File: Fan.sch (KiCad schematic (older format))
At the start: 0 parts

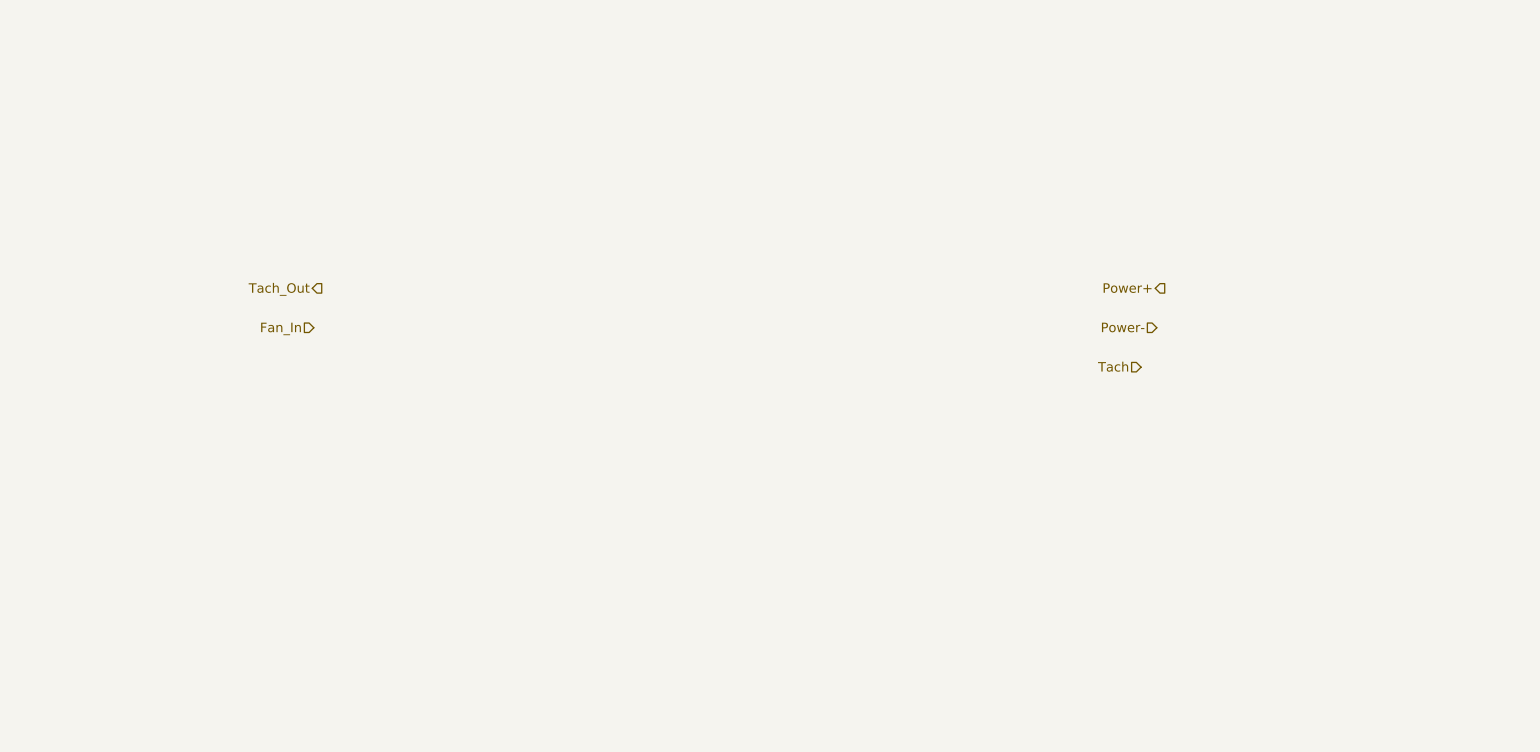
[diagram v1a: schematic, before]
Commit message: Added Fan control outline
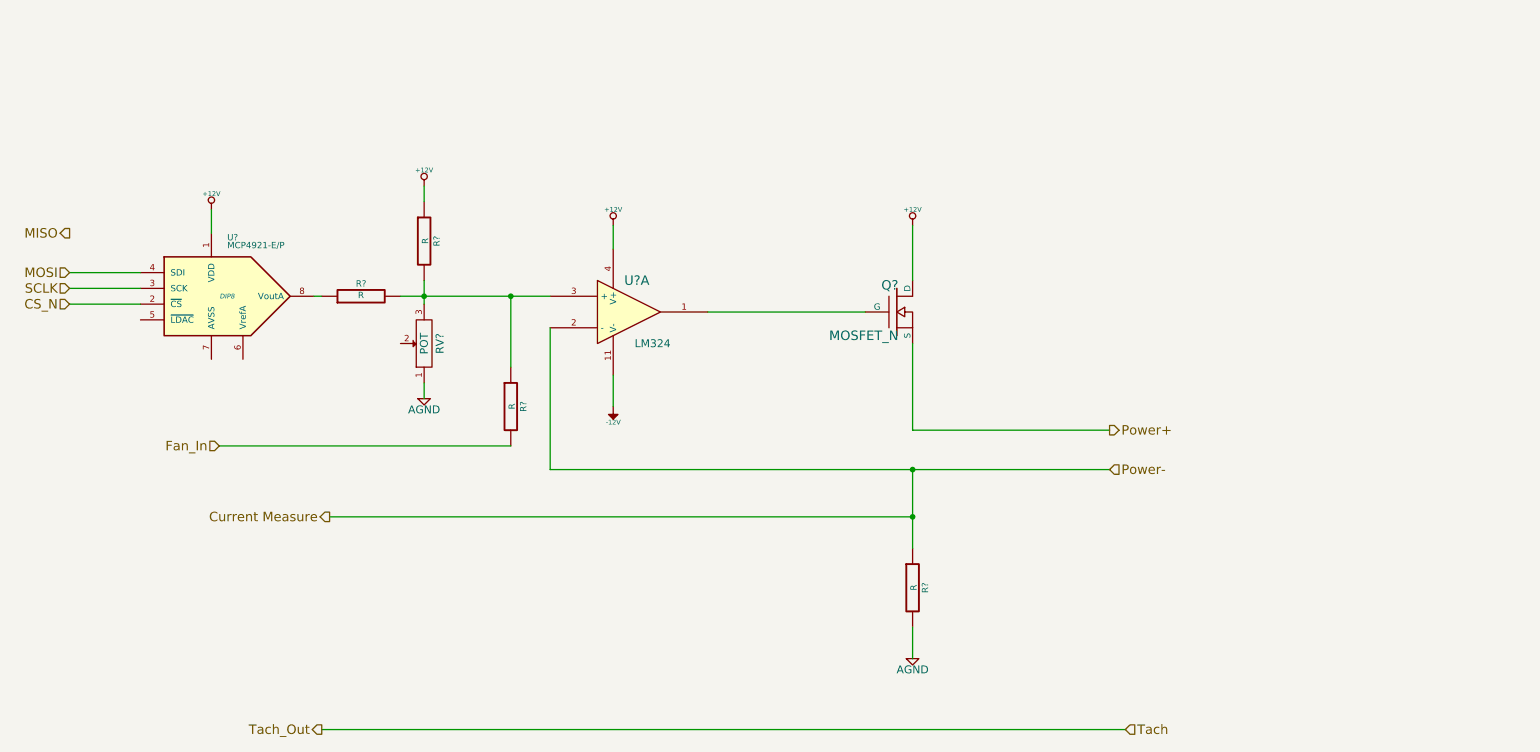
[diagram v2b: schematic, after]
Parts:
- added Q?: MOSFET_N, ~, symbol MOSFET_N
- added R? (x4): R, ~, symbol R
- added RV?: POT, ~, symbol POT
- added U?: LM324, symbol LM324
- added U?: MCP4921-E/P, DIP8, symbol MCP4921-E/P
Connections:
- net Fan_In: now also R?.2
- net Power+: now also Q?.S
- new net: Q?.G, U?.1
- new net: R?.1, R?.2, R?.2, RV?.3, U?.3 (+)
- new net: R?.1, U?.8 (VoutA)
- new net +12V: Q?.D, R?.1, U?.1 (VDD), U?.4 (V+)
- new net -12V: U?.11 (V-)
- new net AGND: R?.2, RV?.1
- new net CS_N: U?.2 (~CS~)
- new net Current Measure: R?.1, U?.2 (-)
- new net MOSI: U?.4 (SDI)
- new net SCLK: U?.3 (SCK)

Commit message: Hooked up top level schematic
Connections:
- net Current Measure renamed CURR_MEAS
- net Fan_In renamed FAN_EN_N
- net Power+ renamed FAN_OUT+
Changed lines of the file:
@@
 $EndDescr
 Text HLabel 7450 3300 2    60   Output ~ 0
-Power+
-Text HLabel 7450 3550 2    60   Input ~ 0
-Power-
+FAN_OUT+
+Text HLabel 7450 3550 2    60   Output ~ 0
+FAN_OUT-
 Text HLabel 7550 5200 2    60   Input ~ 0
-Tach
+TACH_IN
 Text HLabel 2450 5200 0    60   Output ~ 0
-Tach_Out
+TACH_MEAS
 Text HLabel 1800 3400 0    60   Input ~ 0
-Fan_In
+FAN_EN_N
 $Comp
 L LM324 U?
@@
 	2450 5200 7550 5200
 Text HLabel 2500 3850 0    60   Output ~ 0
-Current Measure
+CURR_MEAS
 Wire Wire Line
 	2500 3850 6200 3850

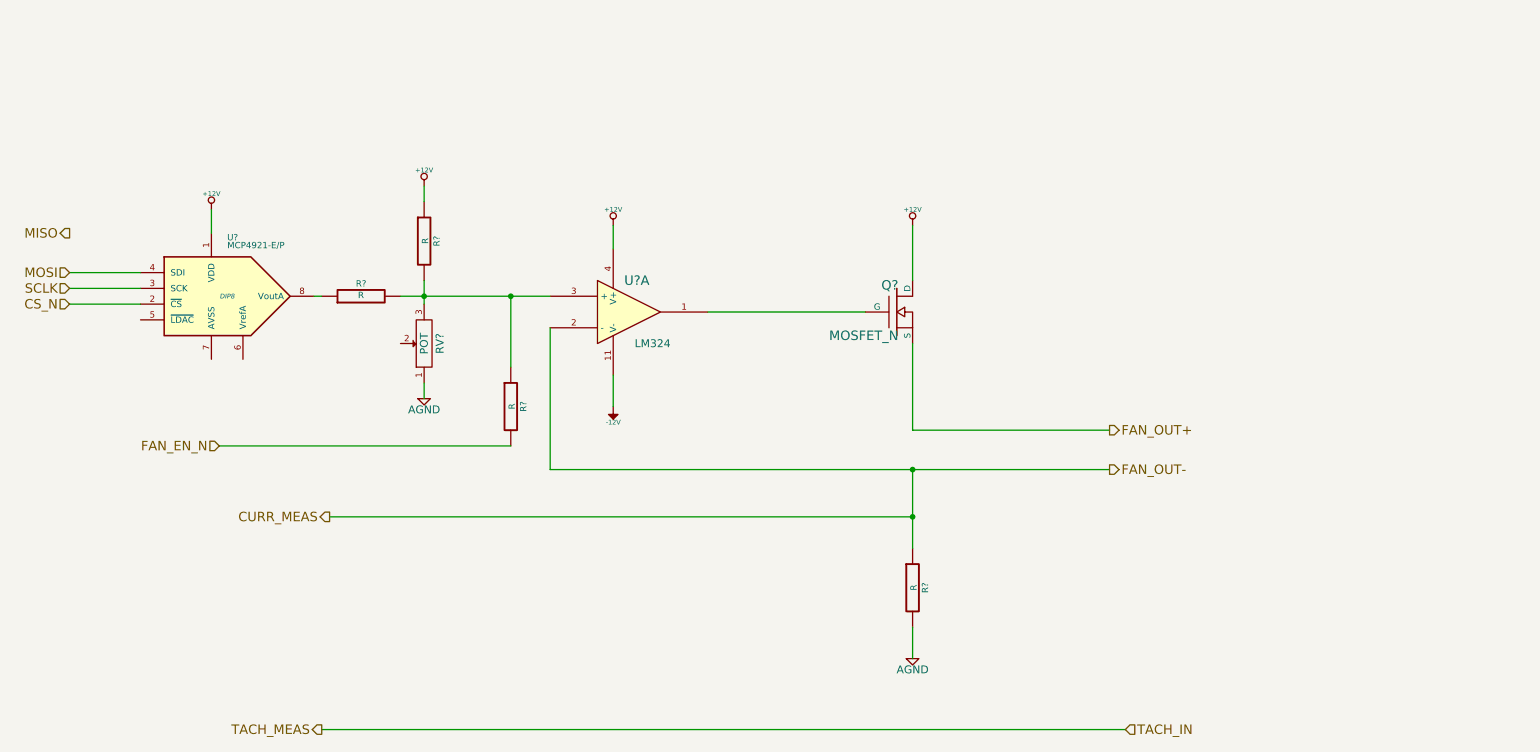
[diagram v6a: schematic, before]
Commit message: Fan Current module refactoring
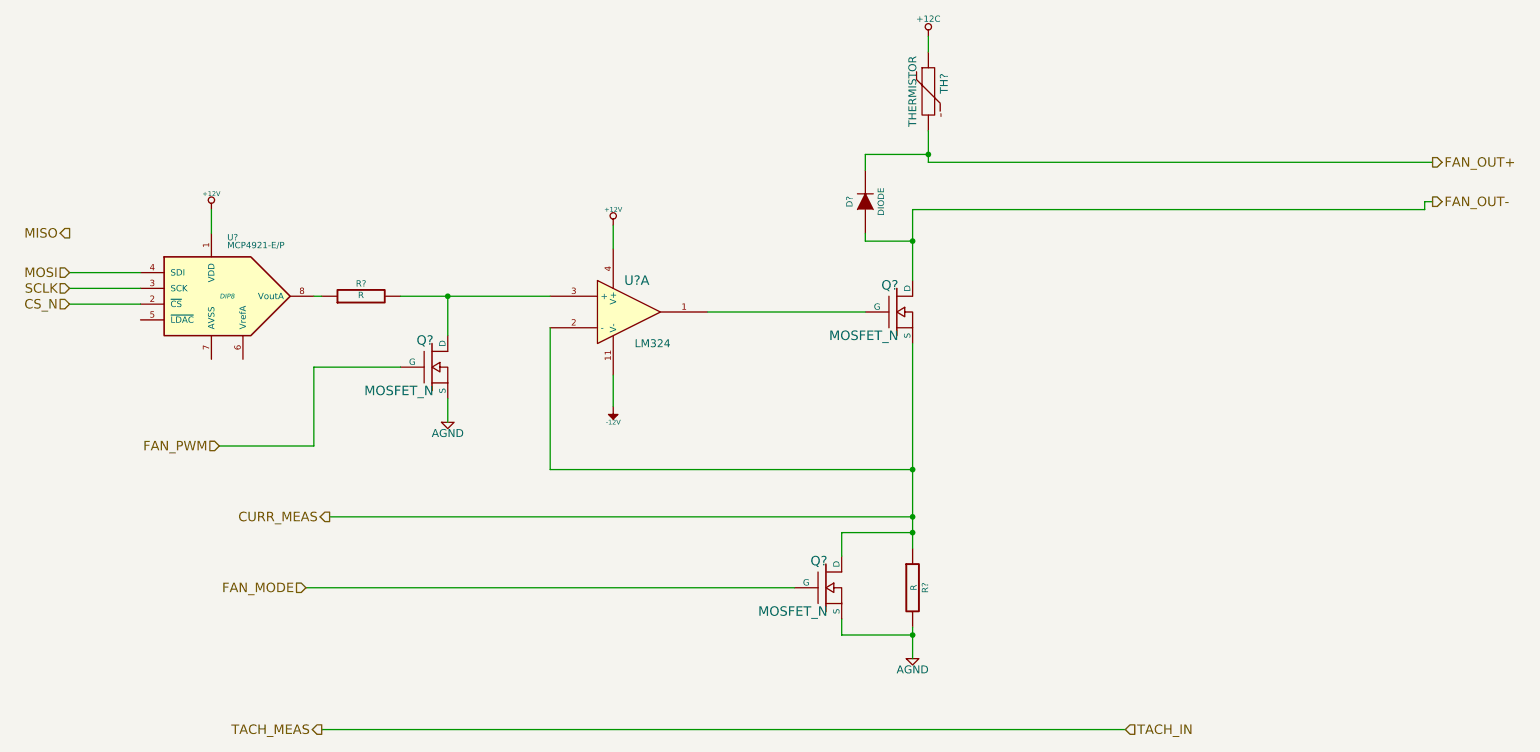
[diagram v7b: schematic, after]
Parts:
- removed R? (x2): R, ~, symbol R
- removed RV?: POT, ~, symbol POT
- added D?: DIODE, ~, symbol DIODE
- added Q? (x2): MOSFET_N, ~, symbol MOSFET_N
- added TH?: THERMISTOR, ~, symbol THERMISTOR
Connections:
- net +12V: no longer Q?.D
- net AGND: now also Q?.S, Q?.S
- net CURR_MEAS: now also Q?.S, Q?.D
- net FAN_OUT+: now also D?.2 (K), TH?.2; no longer Q?.S
- net at R?.2, U?.3 (+): now also Q?.D
- new net +12C: TH?.1
- new net FAN_MODE: Q?.G
- new net FAN_OUT-: D?.1 (A), Q?.D
- new net FAN_PWM: Q?.G
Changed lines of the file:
@@
 $Descr A4 11693 8268
 encoding utf-8
-Sheet 7 9
+Sheet 6 9
 Title ""
 Date "4 feb 2014"
@@
 Comment4 ""
 $EndDescr
-Text HLabel 7450 3300 2    60   Output ~ 0
+Text HLabel 9500 1600 2    60   Output ~ 0
 FAN_OUT+
-Text HLabel 7450 3550 2    60   Output ~ 0
+Text HLabel 9500 1850 2    60   Output ~ 0
 FAN_OUT-
 Text HLabel 7550 5200 2    60   Input ~ 0
@@
 TACH_MEAS
 Text HLabel 1800 3400 0    60   Input ~ 0
-FAN_EN_N
+FAN_PWM
 $Comp
 L LM324 U?
@@
 	1    0    0    -1
 $EndComp
-$Comp
-L +12V #PWR?
-U 1 1 52EF9F16
-P 6200 2000
-F 0 "#PWR?" H 6200 1950 20  0001 C CNN
-F 1 "+12V" H 6200 2100 30  0000 C CNN
-F 2 "" H 6200 2000 60  0000 C CNN
-F 3 "" H 6200 2000 60  0000 C CNN
-	1    6200 2000
-	1    0    0    -1
-$EndComp
-Wire Wire Line
-	6200 2000 6200 2350
+Wire Wire Line
+	6200 1900 6200 2350
 Wire Wire Line
 	4900 2550 5900 2550
 Wire Wire Line
-	6200 2750 6200 3300
-Wire Wire Line
-	6200 3300 7450 3300
-Wire Wire Line
-	3900 3550 6200 3550
-Wire Wire Line
-	6200 3550 7450 3550
-Wire Wire Line
-	6200 3550 6200 3850
-Wire Wire Line
-	6200 3850 6200 4050
+	6200 2750 6200 4050
 $Comp
 L R R?
@@
 	1750 1900 1750 2050
 Wire Wire Line
-	3650 2450 3650 2900
-Connection ~ 3650 2450
-$Comp
-L R R?
-U 1 1 52EFA070
-P 3650 3150
-F 0 "R?" V 3730 3150 40  0000 C CNN
-F 1 "R" V 3657 3151 40  0000 C CNN
-F 2 "~" V 3580 3150 30  0000 C CNN
-F 3 "~" H 3650 3150 30  0000 C CNN
-	1    3650 3150
-	1    0    0    -1
-$EndComp
-Wire Wire Line
-	3650 3400 1800 3400
-$Comp
-L R R?
-U 1 1 52EFA0B3
-P 3100 2100
-F 0 "R?" V 3180 2100 40  0000 C CNN
-F 1 "R" V 3107 2101 40  0000 C CNN
-F 2 "~" V 3030 2100 30  0000 C CNN
-F 3 "~" H 3100 2100 30  0000 C CNN
-	1    3100 2100
-	1    0    0    -1
-$EndComp
-$Comp
-L POT RV?
-U 1 1 52EFA0CB
-P 3100 2750
-F 0 "RV?" H 3100 2650 50  0000 C CNN
-F 1 "POT" H 3100 2750 50  0000 C CNN
-F 2 "~" H 3100 2750 60  0000 C CNN
-F 3 "~" H 3100 2750 60  0000 C CNN
-	1    3100 2750
-	0    -1   -1   0
-$EndComp
-Wire Wire Line
-	2950 2450 3100 2450
-Wire Wire Line
-	3100 2450 3650 2450
-Wire Wire Line
-	3650 2450 3900 2450
-Wire Wire Line
-	3100 2350 3100 2450
-Wire Wire Line
-	3100 2450 3100 2500
-Connection ~ 3100 2450
-$Comp
-L +12V #PWR?
-U 1 1 52EFA14B
-P 3100 1750
-F 0 "#PWR?" H 3100 1700 20  0001 C CNN
-F 1 "+12V" H 3100 1850 30  0000 C CNN
-F 2 "" H 3100 1750 60  0000 C CNN
-F 3 "" H 3100 1750 60  0000 C CNN
-	1    3100 1750
-	1    0    0    -1
-$EndComp
-Wire Wire Line
-	3100 1750 3100 1850
+	2950 2450 3900 2450
 $Comp
 L AGND #PWR?
 U 1 1 52EFA16C
-P 3100 3100
-F 0 "#PWR?" H 3100 3100 40  0001 C CNN
-F 1 "AGND" H 3100 3030 50  0000 C CNN
-F 2 "" H 3100 3100 60  0000 C CNN
-F 3 "" H 3100 3100 60  0000 C CNN
-	1    3100 3100
-	1    0    0    -1
-$EndComp
-Wire Wire Line
-	3100 3000 3100 3100
+P 3250 3250
+F 0 "#PWR?" H 3250 3250 40  0001 C CNN
+F 1 "AGND" H 3250 3180 50  0000 C CNN
+F 2 "" H 3250 3250 60  0000 C CNN
+F 3 "" H 3250 3250 60  0000 C CNN
+	1    3250 3250
+	1    0    0    -1
+$EndComp
 $Comp
 L R R?
@@
 Wire Wire Line
 	2400 2450 2450 2450
+$Comp
+L MOSFET_N Q?
+U 1 1 52F1524F
+P 5650 4300
+F 0 "Q?" H 5660 4470 60  0000 R CNN
+F 1 "MOSFET_N" H 5660 4150 60  0000 R CNN
+F 2 "~" H 5650 4300 60  0000 C CNN
+F 3 "~" H 5650 4300 60  0000 C CNN
+	1    5650 4300
+	1    0    0    -1
+$EndComp
+$Comp
+L THERMISTOR TH?
+U 1 1 52F15270
+P 6300 1150
+F 0 "TH?" V 6400 1200 50  0000 C CNN
+F 1 "THERMISTOR" V 6200 1150 50  0000 C CNN
+F 2 "~" H 6300 1150 60  0000 C CNN
+F 3 "~" H 6300 1150 60  0000 C CNN
+	1    6300 1150
+	1    0    0    -1
+$EndComp
+Wire Wire Line
+	6300 800  6300 900
+Wire Wire Line
+	6300 1400 6300 1600
+Wire Wire Line
+	6300 1600 9500 1600
+$Comp
+L DIODE D?
+U 1 1 52F152D9
+P 5900 1850
+F 0 "D?" H 5900 1950 40  0000 C CNN
+F 1 "DIODE" H 5900 1750 40  0000 C CNN
+F 2 "~" H 5900 1850 60  0000 C CNN
+F 3 "~" H 5900 1850 60  0000 C CNN
+	1    5900 1850
+	0    -1   -1   0
+$EndComp
+Wire Wire Line
+	6200 1900 9450 1900
+Wire Wire Line
+	9450 1900 9450 1850
+Wire Wire Line
+	9450 1850 9500 1850
+Wire Wire Line
+	6200 2100 5900 2100
+Wire Wire Line
+	5900 2100 5900 2050
+Connection ~ 6200 2100
+Wire Wire Line
+	5900 1650 5900 1550
+Wire Wire Line
+	5900 1550 6300 1550
+Connection ~ 6300 1550
+Wire Wire Line
+	3900 3550 6200 3550
+Wire Wire Line
+	6200 3950 5750 3950
+Wire Wire Line
+	5750 3950 5750 4100
+Connection ~ 6200 3950
+Wire Wire Line
+	5750 4500 5750 4600
+Wire Wire Line
+	5750 4600 6200 4600
+Connection ~ 6200 4600
+$Comp
+L MOSFET_N Q?
+U 1 1 52F15414
+P 3150 2900
+F 0 "Q?" H 3160 3070 60  0000 R CNN
+F 1 "MOSFET_N" H 3160 2750 60  0000 R CNN
+F 2 "~" H 3150 2900 60  0000 C CNN
+F 3 "~" H 3150 2900 60  0000 C CNN
+	1    3150 2900
+	1    0    0    -1
+$EndComp
+Wire Wire Line
+	3250 3100 3250 3250
+Wire Wire Line
+	3250 2700 3250 2450
+Connection ~ 3250 2450
+Wire Wire Line
+	1800 3400 2400 3400
+Wire Wire Line
+	2400 3400 2400 2900
+Wire Wire Line
+	2400 2900 2950 2900
+Wire Wire Line
+	5450 4300 2350 4300
+Text HLabel 2350 4300 0    60   Input ~ 0
+FAN_MODE
+$Comp
+L +12C #PWR?
+U 1 1 52F168BA
+P 6300 800
+F 0 "#PWR?" H 6300 770 30  0001 C CNN
+F 1 "+12C" H 6300 910 40  0000 C CNN
+F 2 "" H 6300 800 60  0000 C CNN
+F 3 "" H 6300 800 60  0000 C CNN
+	1    6300 800
+	1    0    0    -1
+$EndComp
 $EndSCHEMATC

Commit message: Begin Associating relay Module
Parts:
- gave numbers to parts that had none: 9
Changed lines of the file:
@@
 LIBS:BenchBudEE
 LIBS:BenchBudEE-cache
-EELAYER 27 0
+EELAYER 24 0
 EELAYER END
 $Descr A4 11693 8268
@@
 FAN_PWM
 $Comp
-L LM324 U?
+L LM324 U7
 U 1 1 52EF9EF8
 P 4400 2550
-F 0 "U?" H 4450 2750 60  0000 C CNN
+F 0 "U7" H 4450 2750 60  0000 C CNN
 F 1 "LM324" H 4550 2350 50  0000 C CNN
 F 2 "" H 4400 2550 60  0000 C CNN
@@
 $EndComp
 $Comp
-L MOSFET_N Q?
+L MOSFET_N Q4
 U 1 1 52EF9F07
 P 6100 2550
-F 0 "Q?" H 6110 2720 60  0000 R CNN
+F 0 "Q4" H 6110 2720 60  0000 R CNN
 F 1 "MOSFET_N" H 6110 2400 60  0000 R CNN
 F 2 "~" H 6100 2550 60  0000 C CNN
@@
 	6200 2750 6200 4050
 $Comp
-L R R?
+L R R17
 U 1 1 52EF9F51
 P 6200 4300
-F 0 "R?" V 6280 4300 40  0000 C CNN
+F 0 "R17" V 6280 4300 40  0000 C CNN
 F 1 "R" V 6207 4301 40  0000 C CNN
 F 2 "~" V 6130 4300 30  0000 C CNN
@@
 $EndComp
 $Comp
-L AGND #PWR?
+L AGND #PWR34
 U 1 1 52EF9F60
 P 6200 4750
-F 0 "#PWR?" H 6200 4750 40  0001 C CNN
+F 0 "#PWR34" H 6200 4750 40  0001 C CNN
 F 1 "AGND" H 6200 4680 50  0000 C CNN
 F 2 "" H 6200 4750 60  0000 C CNN
@@
 	6200 4550 6200 4750
 $Comp
-L +12V #PWR?
+L +12V #PWR32
 U 1 1 52EF9F74
 P 4300 2000
-F 0 "#PWR?" H 4300 1950 20  0001 C CNN
+F 0 "#PWR32" H 4300 1950 20  0001 C CNN
 F 1 "+12V" H 4300 2100 30  0000 C CNN
 F 2 "" H 4300 2000 60  0000 C CNN
@@
 	4300 2000 4300 2150
 $Comp
-L -12V #PWR?
+L -12V #PWR33
 U 1 1 52EF9F84
 P 4300 3150
-F 0 "#PWR?" H 4300 3280 20  0001 C CNN
+F 0 "#PWR33" H 4300 3280 20  0001 C CNN
 F 1 "-12V" H 4300 3250 30  0000 C CNN
 F 2 "" H 4300 3150 60  0000 C CNN
@@
 CS_N
 $Comp
-L MCP4921-E/P U?
+L MCP4921-E/P U6
 U 1 1 52EF9FD5
 P 1850 2450
-F 0 "U?" H 1850 2800 40  0000 L BNN
+F 0 "U6" H 1850 2800 40  0000 L BNN
 F 1 "MCP4921-E/P" H 1850 2750 40  0000 L BNN
 F 2 "DIP8" H 1850 2450 30  0000 C CIN
@@
 	850  2500 1300 2500
 $Comp
-L +12V #PWR?
+L +12V #PWR30
 U 1 1 52EFA03F
 P 1750 1900
-F 0 "#PWR?" H 1750 1850 20  0001 C CNN
+F 0 "#PWR30" H 1750 1850 20  0001 C CNN
 F 1 "+12V" H 1750 2000 30  0000 C CNN
 F 2 "" H 1750 1900 60  0000 C CNN
@@
 	2950 2450 3900 2450
 $Comp
-L AGND #PWR?
+L AGND #PWR31
 U 1 1 52EFA16C
 P 3250 3250
-F 0 "#PWR?" H 3250 3250 40  0001 C CNN
+F 0 "#PWR31" H 3250 3250 40  0001 C CNN
 F 1 "AGND" H 3250 3180 50  0000 C CNN
 F 2 "" H 3250 3250 60  0000 C CNN
@@
 $EndComp
 $Comp
-L R R?
+L R R16
 U 1 1 52EFA195
 P 2700 2450
-F 0 "R?" V 2780 2450 40  0000 C CNN
+F 0 "R16" V 2780 2450 40  0000 C CNN
 F 1 "R" V 2707 2451 40  0000 C CNN
 F 2 "~" V 2630 2450 30  0000 C CNN
@@
 	2400 2450 2450 2450
 $Comp
-L MOSFET_N Q?
+L MOSFET_N Q3
 U 1 1 52F1524F
 P 5650 4300
-F 0 "Q?" H 5660 4470 60  0000 R CNN
+F 0 "Q3" H 5660 4470 60  0000 R CNN
 F 1 "MOSFET_N" H 5660 4150 60  0000 R CNN
 F 2 "~" H 5650 4300 60  0000 C CNN
@@
 $EndComp
 $Comp
-L THERMISTOR TH?
+L THERMISTOR TH5
 U 1 1 52F15270
 P 6300 1150
-F 0 "TH?" V 6400 1200 50  0000 C CNN
+F 0 "TH5" V 6400 1200 50  0000 C CNN
 F 1 "THERMISTOR" V 6200 1150 50  0000 C CNN
 F 2 "~" H 6300 1150 60  0000 C CNN
@@
 	6300 1600 9500 1600
 $Comp
-L DIODE D?
+L DIODE D5
 U 1 1 52F152D9
 P 5900 1850
-F 0 "D?" H 5900 1950 40  0000 C CNN
+F 0 "D5" H 5900 1950 40  0000 C CNN
 F 1 "DIODE" H 5900 1750 40  0000 C CNN
 F 2 "~" H 5900 1850 60  0000 C CNN
@@
 Connection ~ 6200 4600
 $Comp
-L MOSFET_N Q?
+L MOSFET_N Q2
 U 1 1 52F15414
 P 3150 2900
-F 0 "Q?" H 3160 3070 60  0000 R CNN
+F 0 "Q2" H 3160 3070 60  0000 R CNN
 F 1 "MOSFET_N" H 3160 2750 60  0000 R CNN
 F 2 "~" H 3150 2900 60  0000 C CNN
@@
 FAN_MODE
 $Comp
-L +12C #PWR?
+L +12C #PWR35
 U 1 1 52F168BA
 P 6300 800
-F 0 "#PWR?" H 6300 770 30  0001 C CNN
+F 0 "#PWR35" H 6300 770 30  0001 C CNN
 F 1 "+12C" H 6300 910 40  0000 C CNN
 F 2 "" H 6300 800 60  0000 C CNN
